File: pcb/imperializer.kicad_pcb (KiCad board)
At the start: 2 copper layers, 85.1 x 99.1 mm, 24 parts, among them J1 USB_micro_horz_socket_reinfor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, J2 Conn_01x06_Male, SW1 SW_SPST, U1 AS1115-BSST, U2 ATMEGA32U4, U3 LTC-4727, U4 LTC-4727, U5 AP7313, X1 AVR_ISP, Y1 Resonator

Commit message: pcb v1.1
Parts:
- removed J1: USB_micro_horz_socket_reinforced, asl_footprints:microUSB_horizontal_socket
- removed J2: Conn_01x06_Male, Connector_PinHeader_2.54mm:PinHeader_1x06_P2.54mm_Vertical
- removed the S11 at (123.8, 118.1)
- removed U1: AS1115-BSST, Package_SO:QSOP-24_3.9x8.7mm_P0.635mm
- removed the U2 at (96.5, 95.2)
- removed X1: AVR_ISP, asl_footprints:AVR_ISP
- removed Y1: Resonator, Crystal:Resonator_SMD_muRata_CSTxExxV-3Pin_3.0x1.1mm
- added BT1: Battery, Battery:BatteryHolder_Keystone_2466_1xAAA, F.Cu at (96.5, 104.1)
- added BT2: Battery, Battery:BatteryHolder_Keystone_2466_1xAAA, F.Cu at (165.1, 104.1)
- added H1: Threaded_Standoff, asl_footprints:standoff_nut, F.Cu at (92.1, 29.2)
- added H2: Threaded_Standoff, asl_footprints:standoff_nut, F.Cu at (169.5, 132.1)
- added H3: Threaded_Standoff, asl_footprints:standoff_nut, F.Cu at (169.5, 29.2)
- added H4: Threaded_Standoff, asl_footprints:standoff_nut, F.Cu at (92.1, 132.1)
- added R4: 10KΩ, Resistor_SMD:R_0805_2012Metric, B.Cu at (136.7, 50.5)
- added R5: 10KΩ, Resistor_SMD:R_0805_2012Metric, B.Cu at (93.6, 124.5)
- added R6: 10KΩ, Resistor_SMD:R_0805_2012Metric, B.Cu at (93.8, 119.4)
- added R7: 10KΩ, Resistor_SMD:R_0805_2012Metric, B.Cu at (139.5, 41.2)
- added R8: 10KΩ, Resistor_SMD:R_0805_2012Metric, B.Cu at (137.4, 41.2)
- added R9: 10KΩ, Resistor_SMD:R_0805_2012Metric, B.Cu at (136.7, 37.7)
- added S6: switch_momentary_2pin, Button_Switch_Keyboard:SW_Cherry_MX_1.00u_PCB, F.Cu at (152.4, 99.1)
- added U4: trinket_M0, asl_footprints:trinket_M0, F.Cu at (96.5, 121.9)
- added U6: LTC-4727, asl_footprints:LTC-4727, F.Cu at (110.7, 33.8)
- added U7: LTC-4727, asl_footprints:LTC-4727, F.Cu at (150.9, 33.8)
- added U8: AS1115-BSST, Package_SO:QSOP-24_3.9x8.7mm_P0.635mm, B.Cu at (130.8, 34.3)
- R1, R2: value 27Ω -> 10KΩ; moved to B.Cu
- R3: value 25KΩ -> 10KΩ; moved to B.Cu
- S3: footprint Button_Switch_Keyboard:SW_Cherry_MX_1.00u_PCB -> Button_Switch_Keyboard:SW_Cherry_MX_2.00u_PCB
- U5: value AP7313 -> AS1115-BSST; footprint Package_TO_SOT_SMD:TSOT-23 -> Package_SO:QSOP-24_3.9x8.7mm_P0.635mm; moved to B.Cu
- moved R2 46.9 mm to (138.7, 54.4), turned to 270 degrees
- moved R1 42.6 mm to (99.8, 121.9), turned to 0 degrees
- moved U5 42.2 mm to (130.8, 47.0), turned to 270 degrees
- moved R3 38.4 mm to (136.7, 54.4), turned to 270 degrees
- moved S3 34.3 mm to (123.8, 118.1)
- moved SW1 28.8 mm to (165.1, 120.7)
- moved U3 0.63 mm to (150.9, 46.9)
- moved U2 0.51 mm to (110.7, 46.9)
- renumbered S9 to S1, S7 to S10, S8 to S11, S10 to S2, S1 to S4, S2 to S5, S4 to S7, S5 to S8, S6 to S9, U4 to U2
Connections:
- R1 pad 1: Net-(R1-Pad1) -> /VBATT
- R1 pad 2: Net-(J1-PadP3) -> /IRQ
- R2 pad 2: Net-(J1-PadP2) -> /VBATT
- R3 pad 1: /3.3VDC -> Net-(R2-Pad1)
- R3 pad 2: Net-(R3-Pad2) -> /VBATT
- S3 pad 1: /KEYB -> /KEYA
- U5 pad 1: /5VDC -> /SDA
- U5 pad 2: /3.3VDC -> /DIG0
- U5 pad 3: GND -> /DIG1
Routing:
- net /VBATT: track 0.00 -> 158.2 mm, vias 0 -> 6
- net /5VDC: track 130.7 -> 0.00 mm, vias 2 -> 0
- net Net-(BT1-Pad2): track 0.00 -> 113.1 mm, vias 0 -> 2
- net /d2: track 0.00 -> 92.0 mm
- net /3.3VDC: track 90.1 -> 0.00 mm, vias 2 -> 0
- net /g2: track 0.00 -> 78.0 mm, vias 0 -> 2
- net /c2: track 0.00 -> 70.1 mm, vias 0 -> 1
- net /f2: track 0.00 -> 66.4 mm, vias 0 -> 2
- net /a2: track 0.00 -> 64.8 mm, vias 0 -> 2
- net /b2: track 0.00 -> 58.5 mm, vias 0 -> 1
- net /DIG7: track 90.6 -> 37.1 mm
- net /DIG6: track 88.4 -> 35.8 mm, vias 3 -> 2
- net /DIG4: track 68.7 -> 18.7 mm
- net /e2: track 0.00 -> 48.3 mm, vias 0 -> 3
- net /KEYB: track 197.4 -> 151.4 mm, vias 3 -> 1
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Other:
- board size 85.1 x 99.1 mm -> 85.2 x 110.5 mm
- board text added: "Imperializer v1.1"
- board text removed: "5V"
- board text removed: "GND"
- board text removed: "IRQ"
- board text removed: "Mode"
- board text removed: "SCL"
- board text removed: "SDA"

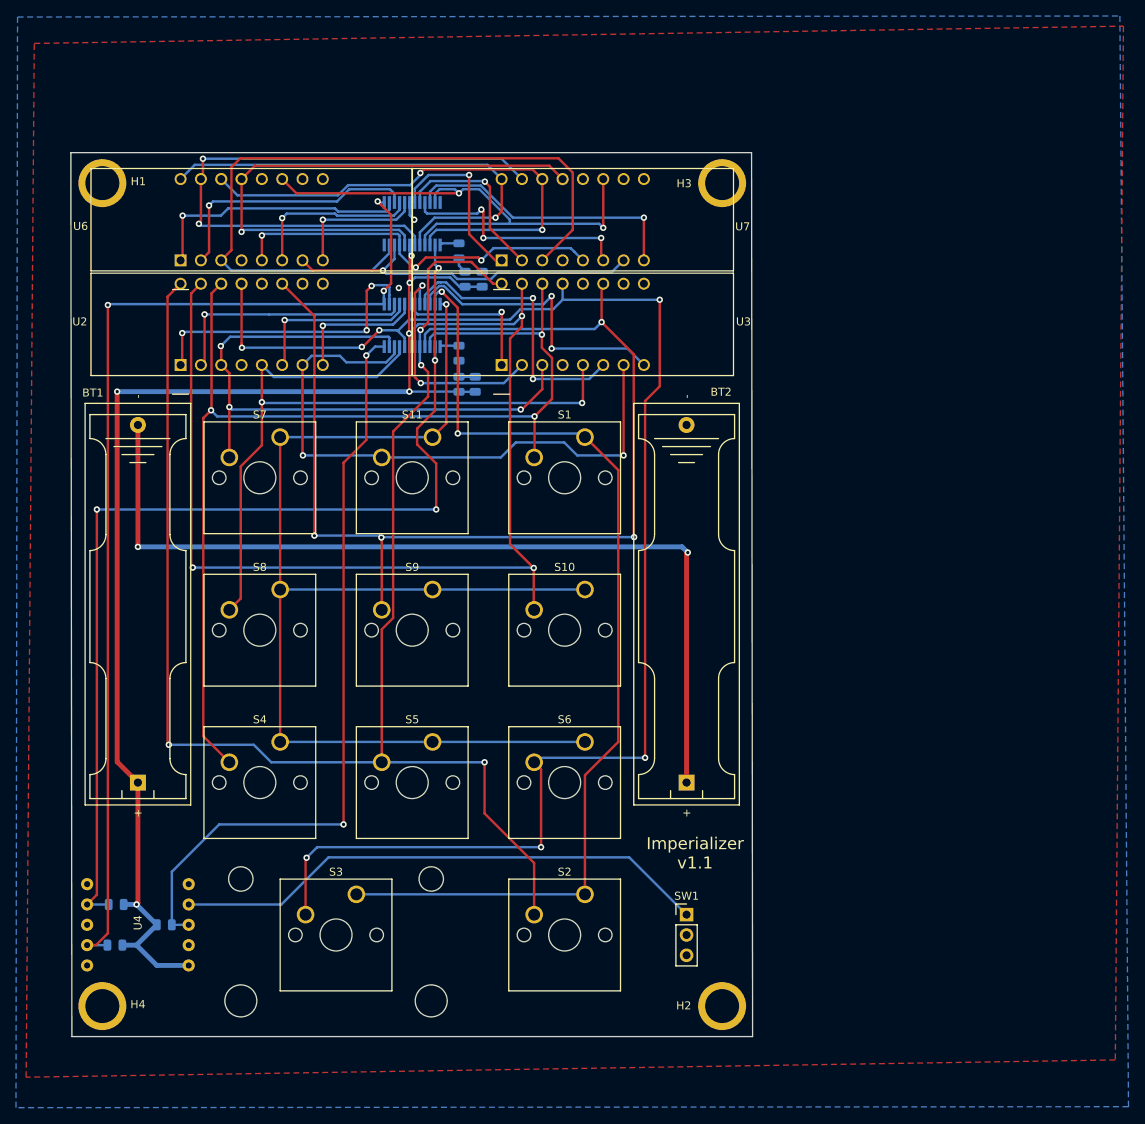
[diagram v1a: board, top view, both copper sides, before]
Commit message: pcb v1.2
switched to bare SAMD21
added USB-C connector
added 4 conversion selection LEDs
added on/off button with soft latch circuit
rearranged toggles switch and battery holders
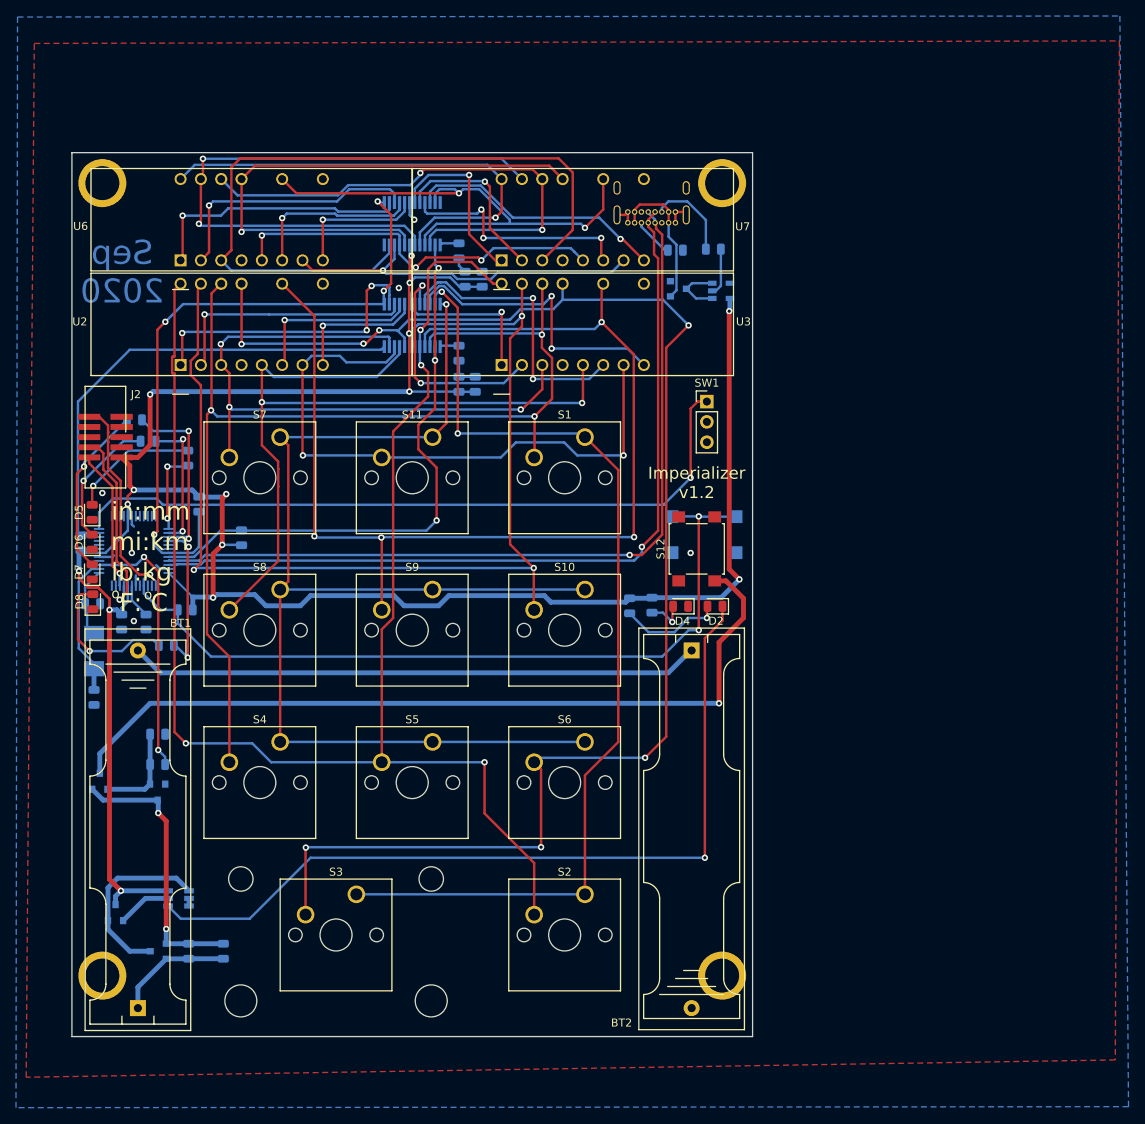
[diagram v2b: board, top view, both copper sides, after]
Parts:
- added C1: 15pF, Capacitor_SMD:C_0805_2012Metric, B.Cu at (90.9, 81.8)
- added C2: 15pF, Capacitor_SMD:C_0805_2012Metric, B.Cu at (91.0, 93.5)
- added C3: 0.1µF, Capacitor_SMD:C_0805_2012Metric, B.Cu at (97.5, 84.1)
- added C4: 0.1µF, Capacitor_SMD:C_0805_2012Metric, B.Cu at (94.5, 84.1)
- added C5: 10nF, Capacitor_SMD:C_0805_2012Metric, B.Cu at (102.9, 125.2)
- added D1: BAT54C, Package_TO_SOT_SMD:SOT-23, B.Cu at (91.8, 104.0)
- added D2: LED, LED_SMD:LED_0805_2012Metric, F.Cu at (168.7, 82.1)
- added D3: BAT54C, Package_TO_SOT_SMD:SOT-23, B.Cu at (164.1, 42.4)
- added D4: LED, LED_SMD:LED_0805_2012Metric, F.Cu at (164.4, 82.1)
- added D5: LED, LED_SMD:LED_0805_2012Metric, F.Cu at (90.8, 70.4)
- added D6: LED, LED_SMD:LED_0805_2012Metric, F.Cu at (90.8, 74.1)
- added D7: LED, LED_SMD:LED_0805_2012Metric, F.Cu at (90.8, 77.8)
- added D8: LED, LED_SMD:LED_0805_2012Metric, F.Cu at (90.9, 81.5)
- added J1: USB_C_Receptacle_USB2.0, asl_footprints:USB_C_Receptacle_GCT_USB4085, B.Cu at (157.8, 34.2)
- added J2: SWD_connector, asl_footprints:SWD_2x5_socket, F.Cu at (92.5, 61.0)
- added Q1: FDN340P, Package_TO_SOT_SMD:SOT-23, B.Cu at (99.1, 125.2)
- added Q2: BSS123, Package_TO_SOT_SMD:SOT-23, B.Cu at (99.0, 105.3)
- added Q3: FDN340P, Package_TO_SOT_SMD:SOT-23, B.Cu at (93.7, 120.4)
- added R10: 10KΩ, Resistor_SMD:R_0805_2012Metric, B.Cu at (102.4, 82.5)
- added R11: 100KΩ, Resistor_SMD:R_0805_2012Metric, B.Cu at (107.2, 125.2)
- added R12: 330KΩ, Resistor_SMD:R_0805_2012Metric, B.Cu at (99.0, 101.9)
- added R13: 1MΩ, Resistor_SMD:R_0805_2012Metric, B.Cu at (99.0, 98.1)
- added R14: 5.1KΩ, Resistor_SMD:R_0805_2012Metric, B.Cu at (163.7, 37.6)
- added R15: 5.1KΩ, Resistor_SMD:R_0805_2012Metric, B.Cu at (168.5, 37.5)
- added R16: 330KΩ, Resistor_SMD:R_0805_2012Metric, B.Cu at (158.0, 82.0)
- added R17: 330KΩ, Resistor_SMD:R_0805_2012Metric, B.Cu at (160.8, 82.0)
- added R18: 10KΩ, Resistor_SMD:R_0805_2012Metric, B.Cu at (102.7, 63.6)
- added R19: 10KΩ, Resistor_SMD:R_0805_2012Metric, B.Cu at (97.8, 61.5)
- added R20: 10KΩ, Resistor_SMD:R_0805_2012Metric, B.Cu at (96.1, 58.8)
- added R21: 10KΩ, Resistor_SMD:R_0805_2012Metric, B.Cu at (100.1, 87.0)
- added S12: B3FS-1010P, asl_footprints:6mm_tactile_smd, F.Cu at (166.4, 74.9)
- added S13: B3FS-1010P, asl_footprints:6mm_tactile_smd, B.Cu at (167.4, 73.2)
- added U1: ATSAMD21G15A-A, Package_QFP:TQFP-48_7x7mm_P0.5mm, B.Cu at (96.0, 75.2)
- added U9: LTC4412xS6, Package_TO_SOT_SMD:TSOT-23-6, B.Cu at (101.6, 118.6)
- added Y1: Crystal, Crystal:Crystal_SMD_0603-2Pin_6.0x3.5mm, B.Cu at (91.0, 87.7)
- SW1: footprint Connector_PinHeader_2.54mm:PinHeader_1x03_P2.54mm_Vertical -> asl_footprints:B12AP
- U4: value trinket_M0 -> AP2112K-3.3; footprint asl_footprints:trinket_M0 -> Package_TO_SOT_SMD:SOT-23-5; moved to B.Cu
- moved U4 107.7 mm to (169.4, 42.7), turned to 0 degrees
- moved SW1 64.2 mm to (167.6, 56.5)
- moved R5 56.1 mm to (104.1, 69.3), turned to 90 degrees
- moved R1 48.9 mm to (89.4, 74.2), turned to 90 degrees
- moved R6 48.5 mm to (109.5, 73.5), turned to 270 degrees
- moved BT1 28.2 mm to (96.5, 132.3)
- moved BT2 16.5 mm to (165.7, 87.6), turned to 270 degrees
- moved H2 3.81 mm to (169.5, 128.3)
- moved H4 3.81 mm to (92.1, 128.3)
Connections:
- R1 pad 1: /VBATT -> /VIN
- R2 pad 2: /VBATT -> /VIN
- R3 pad 2: /VBATT -> /VIN
- R5 pad 2: /VBATT -> /VIN
- R6 pad 2: /VBATT -> /VIN
- R7 pad 2: /VBATT -> /VIN
- R8 pad 2: /VBATT -> /VIN
- U4 pad 1: /VBATT -> Net-(D3-Pad3)
- U4 pad 3: /IRQ -> Net-(D3-Pad3)
- U4 pad 4: /mode -> (no net)
- U4 pad 5: (no net) -> /VIN
- U5 pad 19: /VBATT -> /VIN
- U8 pad 19: /VBATT -> /VIN
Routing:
- net /VIN: track 0.00 -> 299.3 mm, vias 0 -> 15
- net /VBATT: track 158.2 -> 14.8 mm, vias 6 -> 0
- net /RST: track 0.00 -> 124.5 mm, vias 0 -> 3
- net /D-: track 0.00 -> 104.1 mm, vias 0 -> 1
- net /D+: track 0.00 -> 104.1 mm, vias 0 -> 1
- net Net-(D2-Pad1): track 0.00 -> 103.3 mm, vias 0 -> 1
- net Net-(D1-Pad3): track 0.00 -> 101.3 mm, vias 0 -> 1
- net /SCL: track 132.1 -> 73.7 mm, vias 4 -> 3
- net /SDA: track 133.7 -> 82.2 mm, vias 3 -> 4
- net Net-(BT1-Pad2): track 113.1 -> 71.5 mm, vias 2 -> 0
- net /IRQ: track 95.2 -> 60.4 mm, vias 2 -> 0
- net Net-(C5-Pad2): track 0.00 -> 34.3 mm, vias 0 -> 2
- net /BTN: track 0.00 -> 33.1 mm, vias 0 -> 2
- net /SWCLK: track 0.00 -> 25.0 mm, vias 0 -> 1
- net Net-(Q1-Pad3): track 0.00 -> 22.9 mm
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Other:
- board size 85.2 x 110.5 mm -> 85.1 x 110.5 mm
- board text added: "C"
- board text added: "F:"
- board text added: "Imperializer v1.2"
- board text added: "RST"
- board text added: "Sep 2020"
- board text added: "in:mm"
- board text added: "lb:kg"
- board text added: "mi:km"
- board text added: "o"
- board text removed: "Imperializer v1.1"

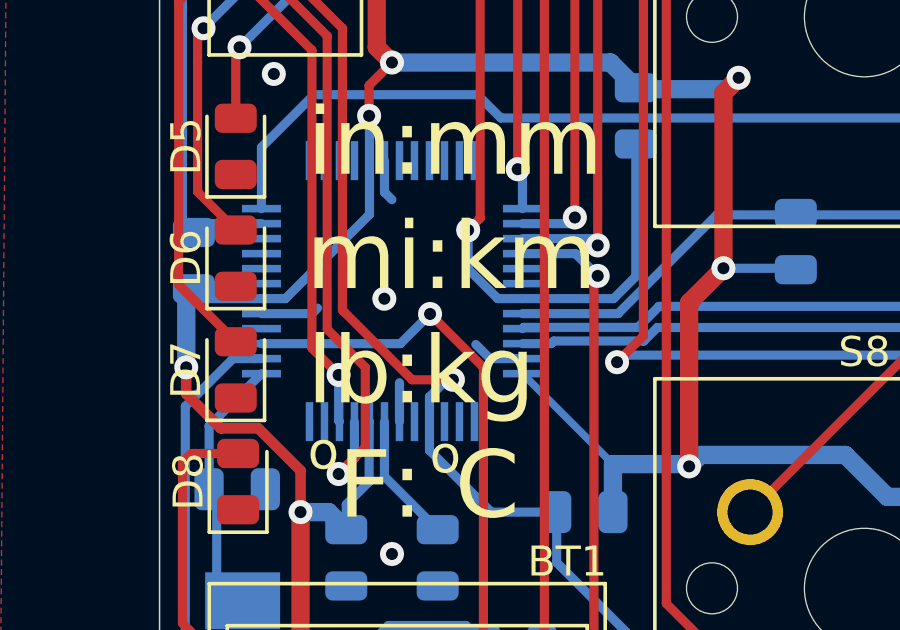
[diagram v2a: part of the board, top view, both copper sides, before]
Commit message: Kicad update
updated to kicad 5.99 nightly. There is now a new file format
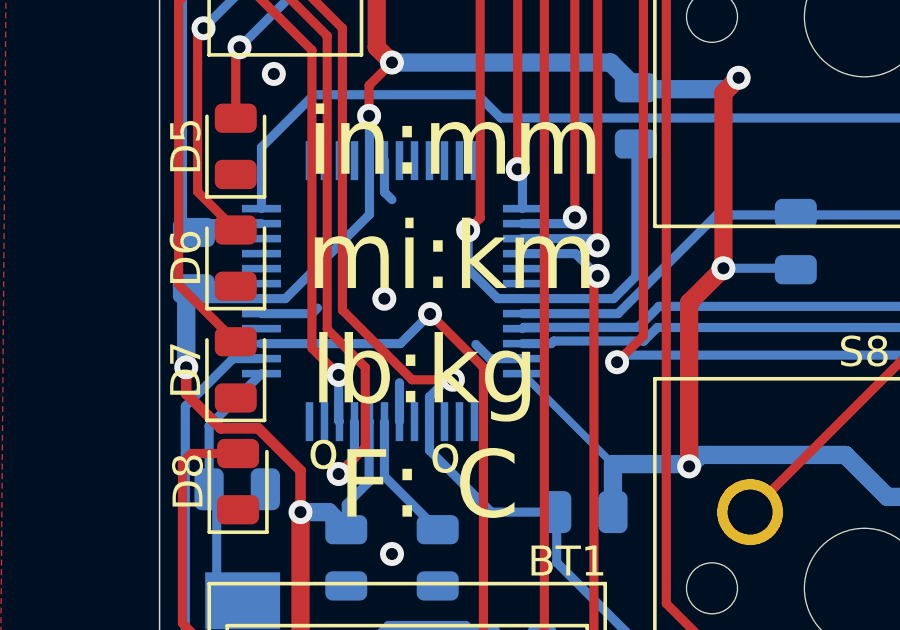
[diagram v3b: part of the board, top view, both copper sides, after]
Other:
- net class Default removed
- net class POWER removed

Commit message: pcb v1.3
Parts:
- removed BT2: Battery, Battery:BatteryHolder_Keystone_2466_1xAAA
- removed C1, C2: 15pF, Capacitor_SMD:C_0805_2012Metric
- removed H1, H2, H3, H4: Threaded_Standoff, asl_footprints:standoff_nut
- removed J1: USB_C_Receptacle_USB2.0, asl_footprints:USB_C_Receptacle_GCT_USB4085
- removed Q3: FDN340P, Package_TO_SOT_SMD:SOT-23
- removed R16: 330KΩ, Resistor_SMD:R_0805_2012Metric
- removed U4: AP2112K-3.3, Package_TO_SOT_SMD:SOT-23-5
- removed U9: LTC4412xS6, Package_TO_SOT_SMD:TSOT-23-6
- removed Y1: Crystal, Crystal:Crystal_SMD_0603-2Pin_6.0x3.5mm
- added L1: 10µH, Inductor_SMD:L_0805_2012Metric, B.Cu at (97.6, 117.6)
- added S14: Gateron Blue, Button_Switch_Keyboard:SW_Cherry_MX_1.00u_PCB, F.Cu at (171.4, 99.1)
- added S15: Gateron Blue, Button_Switch_Keyboard:SW_Cherry_MX_1.00u_PCB, F.Cu at (171.4, 80.0)
- added U10: ATSAMD21E15A-A, Package_QFP:TQFP-32_7x7mm_P0.8mm, B.Cu at (96.6, 75.1)
- BT1: value Battery -> 2466
- D3: value BAT54C -> LED; footprint Package_TO_SOT_SMD:SOT-23 -> LED_SMD:LED_0805_2012Metric; moved to F.Cu
- J2: value SWD_connector -> SHF-105-01-L-D-SM
- R12: value 330KΩ -> 330Ω
- R14, R15: value 5.1KΩ -> 470Ω
- R18, R19, R20, R21: value 10KΩ -> 470Ω
- S1, S10, S11, S2, S3, S4, S5, S6, S7, S8, S9: value switch_momentary_2pin -> Gateron Blue
- S12: value B3FS-1010P -> Gateron Blue; footprint asl_footprints:6mm_tactile_smd -> Button_Switch_Keyboard:SW_Cherry_MX_1.00u_PCB
- S13: moved to F.Cu
- U1: value ATSAMD21G15A-A -> MAX1724; footprint Package_QFP:TQFP-48_7x7mm_P0.5mm -> Package_TO_SOT_SMD:SOT-23-5
- U2, U3: value LTC-4727 -> LTC-4727JS
- U6, U7: value LTC-4727 -> LTC-4727JR
- moved J2 86.9 mm to (175.0, 33.8)
- moved R15 80.1 mm to (91.5, 59.8), turned to 180 degrees
- moved D2 79.4 mm to (90.8, 66.6), turned to 90 degrees
- moved D4 77.4 mm to (90.9, 57.6), turned to 90 degrees
- moved D3 76.1 mm to (90.8, 62.8), turned to 90 degrees
- moved R17 72.1 mm to (94.0, 54.9), turned to 180 degrees
- moved R14 71.4 mm to (97.8, 65.0), turned to 180 degrees
- moved U1 46.8 mm to (97.6, 122.0), turned to 180 degrees
- moved S12 43.5 mm to (171.4, 118.1), turned to 0 degrees
- moved S13 27.3 mm to (174.8, 46.9), turned to -90 degrees
- moved C5 15.9 mm to (95.6, 111.0)
- moved Q1 15.9 mm to (91.8, 111.0)
- moved R11 15.9 mm to (99.9, 111.0)
- moved SW1 7.34 mm to (169.9, 63.5)
- moved BT1 1.62 mm to (94.9, 132.2)
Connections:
- BT1 pad 2: Net-(BT1-Pad2) -> GND
- C5 pad 1: /VBATT -> Net-(C5-Pad1)
- D1 pad 3: Net-(D1-Pad3) -> GND
- D2 pad 1: Net-(D2-Pad1) -> GND
- D3 pad 1: /VUSB -> GND
- D3 pad 2: (no net) -> Net-(D3-Pad2)
- Q1 pad 2: /VBATT -> Net-(C5-Pad1)
- Q1 pad 3: Net-(Q1-Pad3) -> /VIN
- R11 pad 2: /VBATT -> Net-(C5-Pad1)
- R14 pad 2: GND -> Net-(D2-Pad2)
- R15 pad 2: GND -> Net-(D3-Pad2)
- S12 pad 1: (no net) -> GND
- S12 pad 2: Net-(D1-Pad3) -> GND
- U1 pad 1: Net-(C1-Pad1) -> /VBATT
- U1 pad 2: Net-(C2-Pad2) -> GND
- U1 pad 3: /BTN -> /VBATT
- U1 pad 4: (no net) -> Net-(C5-Pad1)
- U1 pad 5: GND -> Net-(L1-Pad2)
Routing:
- net /SWDIO: track 17.6 -> 127.7 mm, vias 1 -> 3
- net /D-: track 104.1 -> 0.00 mm, vias 1 -> 0
- net /D+: track 104.1 -> 0.00 mm, vias 1 -> 0
- net Net-(D2-Pad1): track 103.3 -> 0.00 mm, vias 1 -> 0
- net Net-(D1-Pad3): track 101.3 -> 0.00 mm, vias 1 -> 0
- net /SWCLK: track 25.0 -> 123.5 mm, vias 1 -> 3
- net Net-(BT1-Pad2): track 71.5 -> 0.00 mm
- net /d: track 80.5 -> 145.5 mm, vias 3 -> 4
- net /e: track 98.8 -> 137.3 mm, vias 2 -> 3
- net /KEYA: track 126.0 -> 159.9 mm, vias 2 -> 3
- net Net-(Q1-Pad3): track 22.9 -> 0.00 mm
- net Net-(C5-Pad1): track 0.00 -> 20.1 mm
- net /RST: track 124.5 -> 143.1 mm, vias 3 -> 1
- net /VUSB: track 17.9 -> 0.00 mm
- net Net-(C2-Pad2): track 17.5 -> 0.00 mm
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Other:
- board size 85.1 x 110.5 mm -> 90.8 x 110.5 mm
- board text added: "Imperializer v1.3"
- board text added: "Oct 2020"
- board text added: "ft:m"
- board text added: "oz:mL"
- board text removed: "Imperializer v1.2"
- board text removed: "Sep 2020"
